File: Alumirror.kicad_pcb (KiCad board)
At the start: 2 copper layers, 139.7 x 88.9 mm, 96 parts, among them J1 USB_C_Receptacle_USB2.0_16P_2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, J2 USB_C_Receptacle_USB2.0_16P_2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, J3 USB_C_Receptacle_USB2.0_16P_2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, J4 USB_C_Receptacle_USB2.0_16P_2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, K11 PG1350, K12 PG1350, K13 PG1350, K14 PG1350, K15 PG1350, K16 PG1350, K21 PG1350, K22 PG1350, K23 PG1350, K24 PG1350, K25 PG1350, K26 PG1350, K31 PG1350, K32 PG1350, K33 PG1350, K34 PG1350, K35 PG1350, K36 PG1350_1½U, K41 PG1350_1½U, K42 PG1350/SKQUCAA010, SW10 BOOT, U1 CH552T, U2 CH552T, U3 USBLC6-2P6, U4 USBLC6-2P6, U5 USBLC6-2P6, U6 USBLC6-2P6

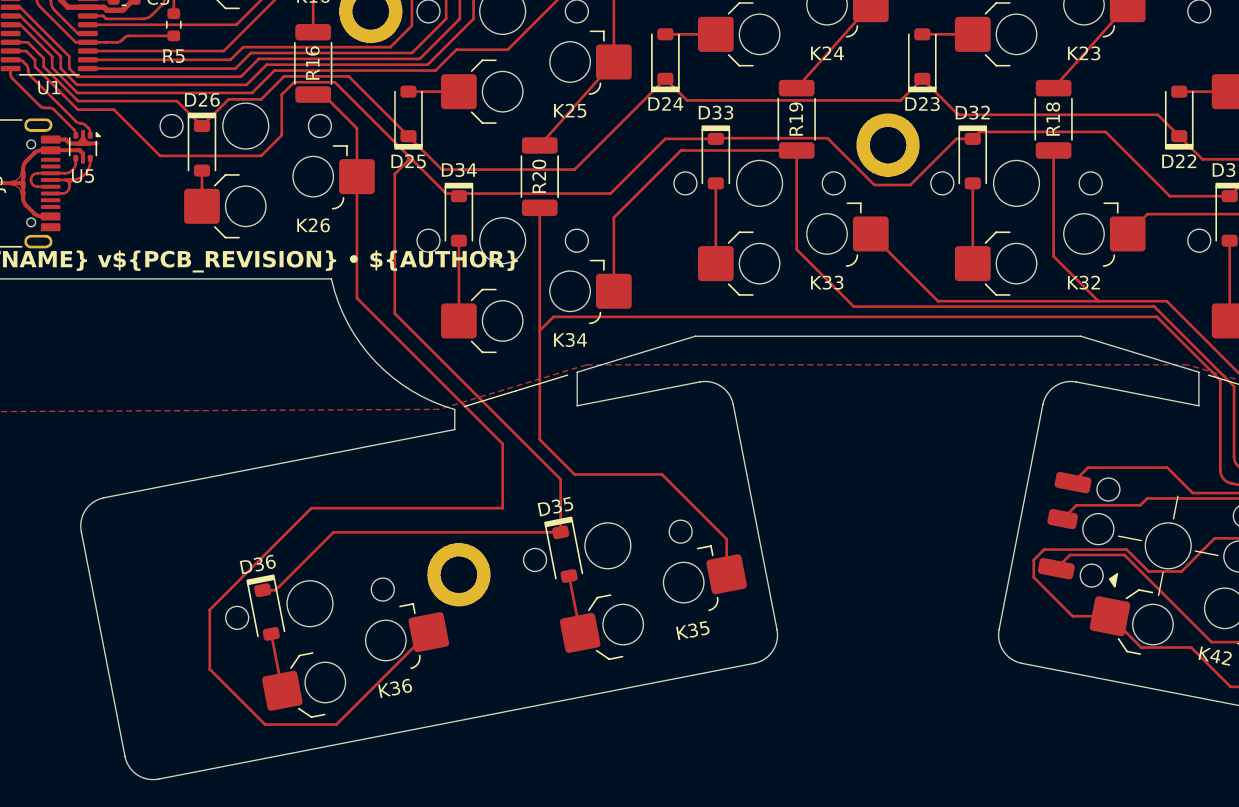
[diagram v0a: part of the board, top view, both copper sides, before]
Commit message: Clean up left thumb traces
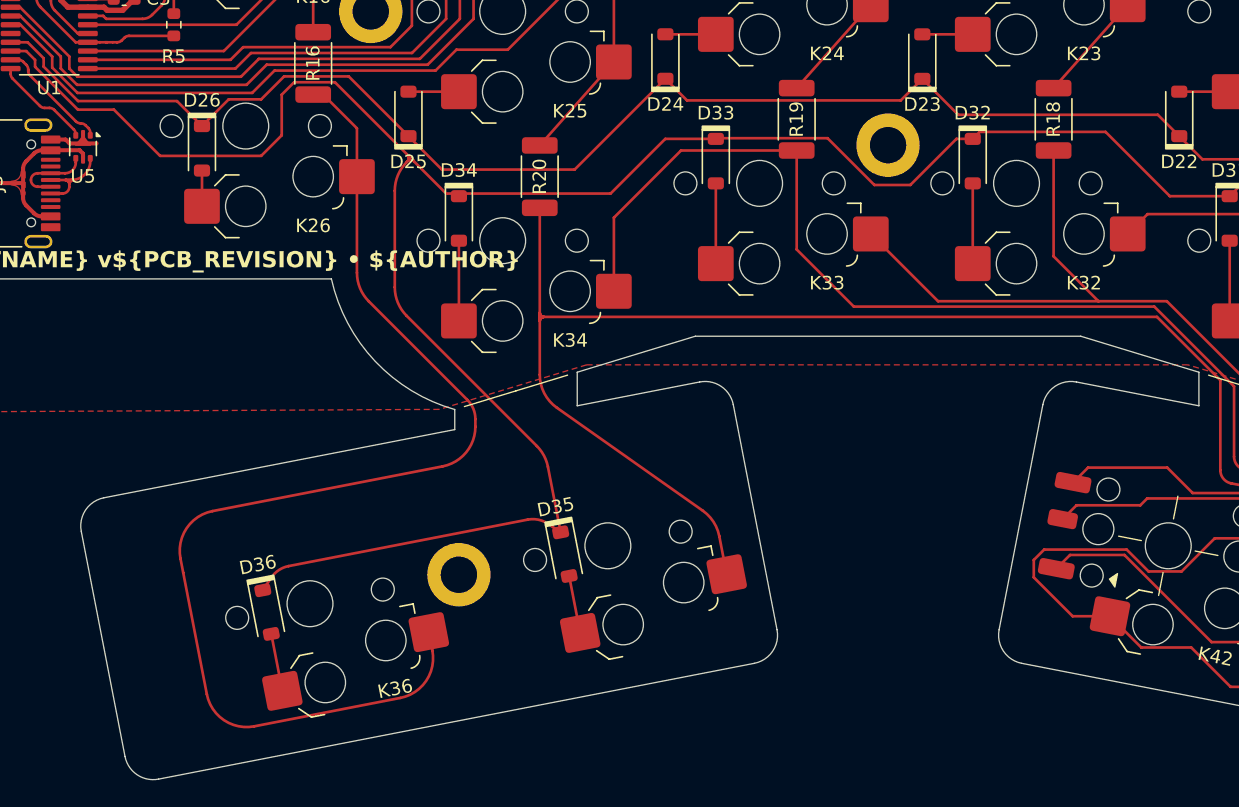
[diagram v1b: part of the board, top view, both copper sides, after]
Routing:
- net Col5T: track 113.3 -> 109.8 mm
- net Col6T: track 86.3 -> 87.1 mm
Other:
- board text added: "LED"

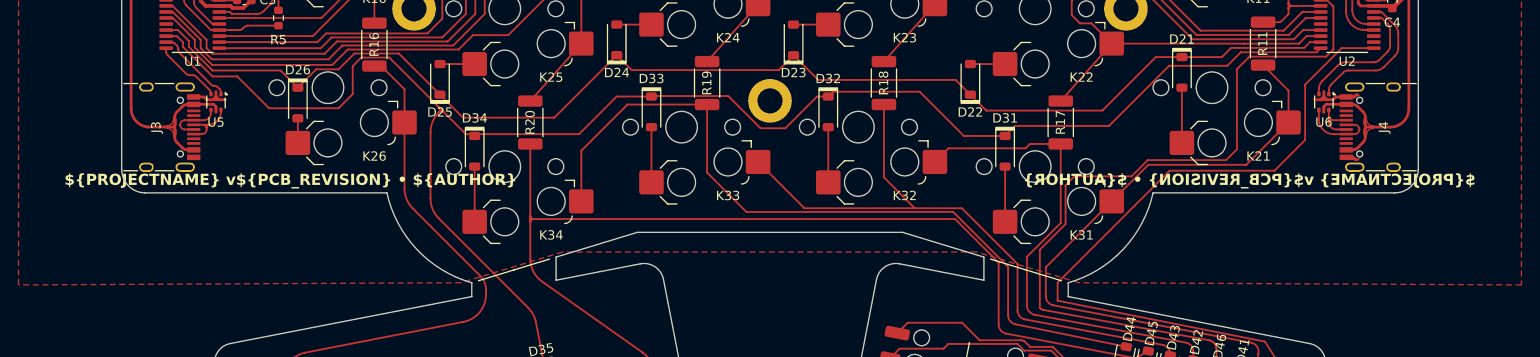
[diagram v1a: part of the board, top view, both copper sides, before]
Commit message: Switch label to mask instead of silkscreen
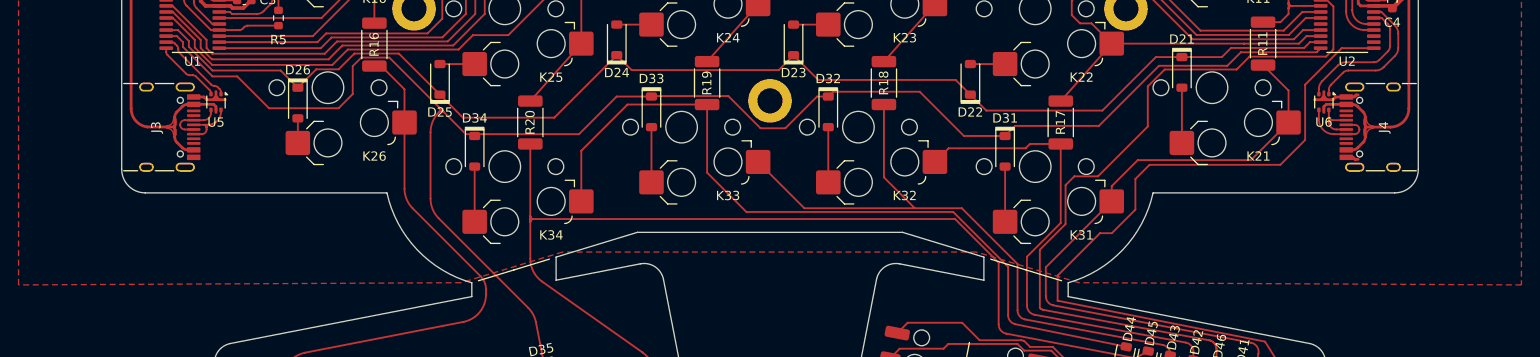
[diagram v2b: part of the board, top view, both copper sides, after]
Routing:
- net Col6: track 228.2 -> 225.7 mm
- net Row4R: track 170.3 -> 172.6 mm
- net Col1T: track 79.9 -> 80.8 mm

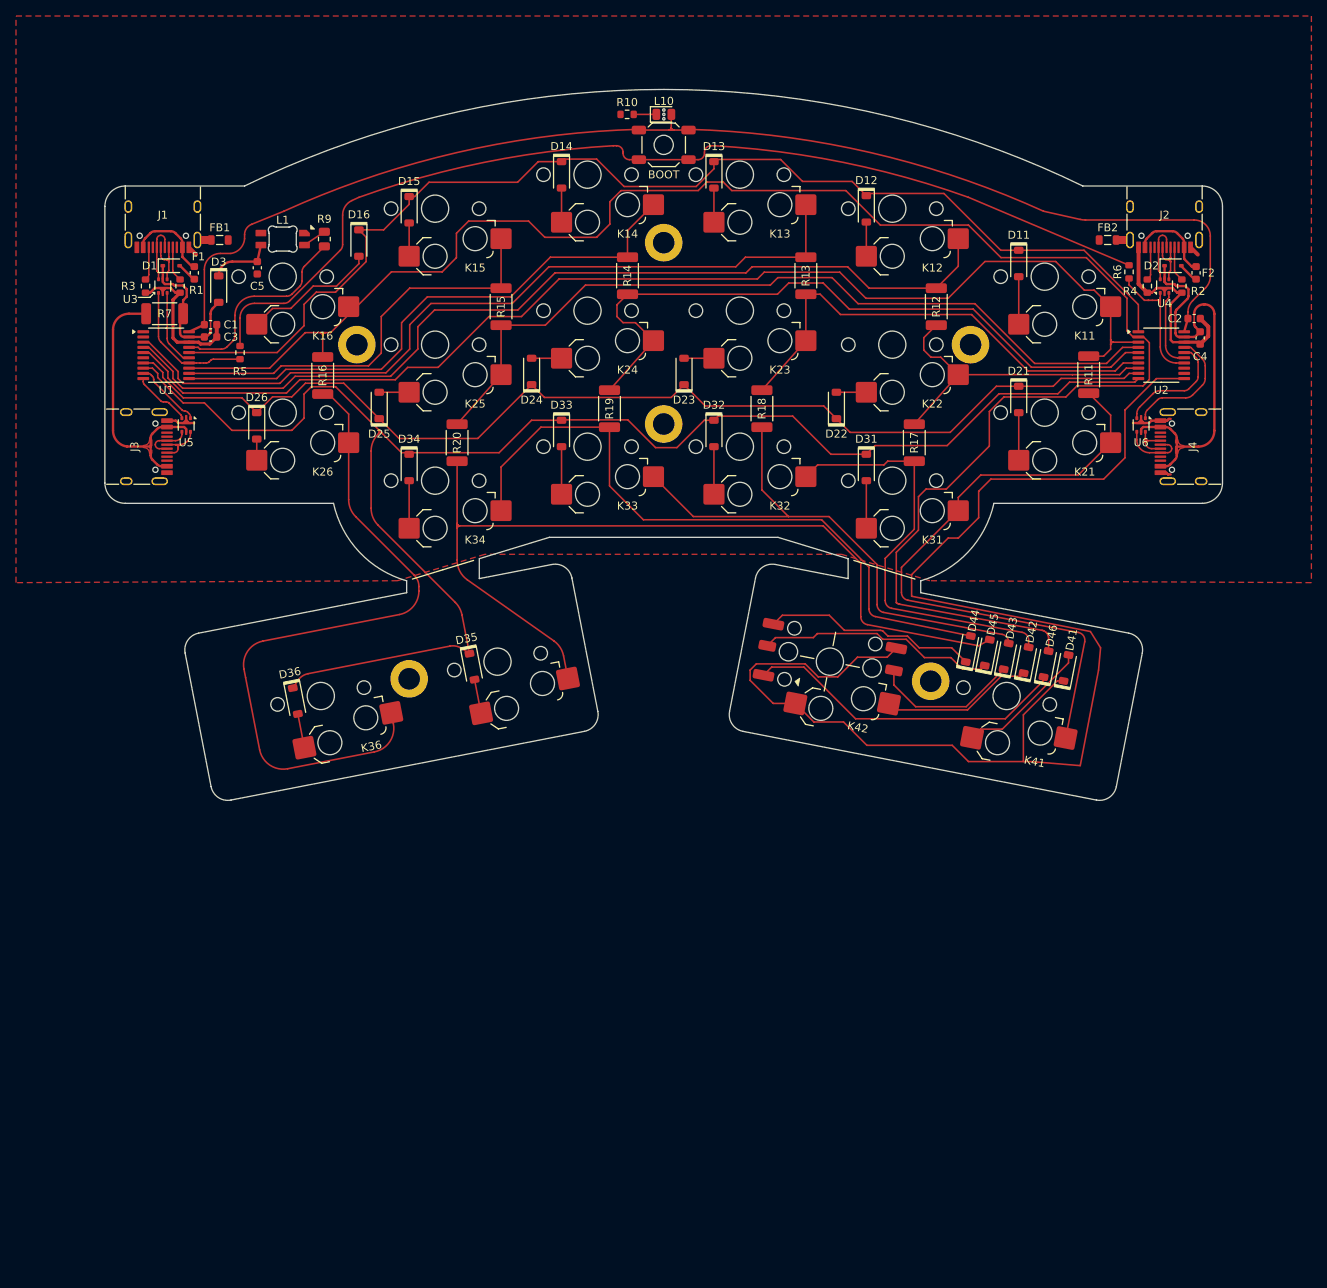
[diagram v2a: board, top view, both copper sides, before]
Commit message: Switch K22 to new “clipped” footprint
Clipped footprint has a cut-out in one of the hot-swap socket pads to avoid proximity warning with solder nut pad.
Also tweaked and rounded multiple traces.
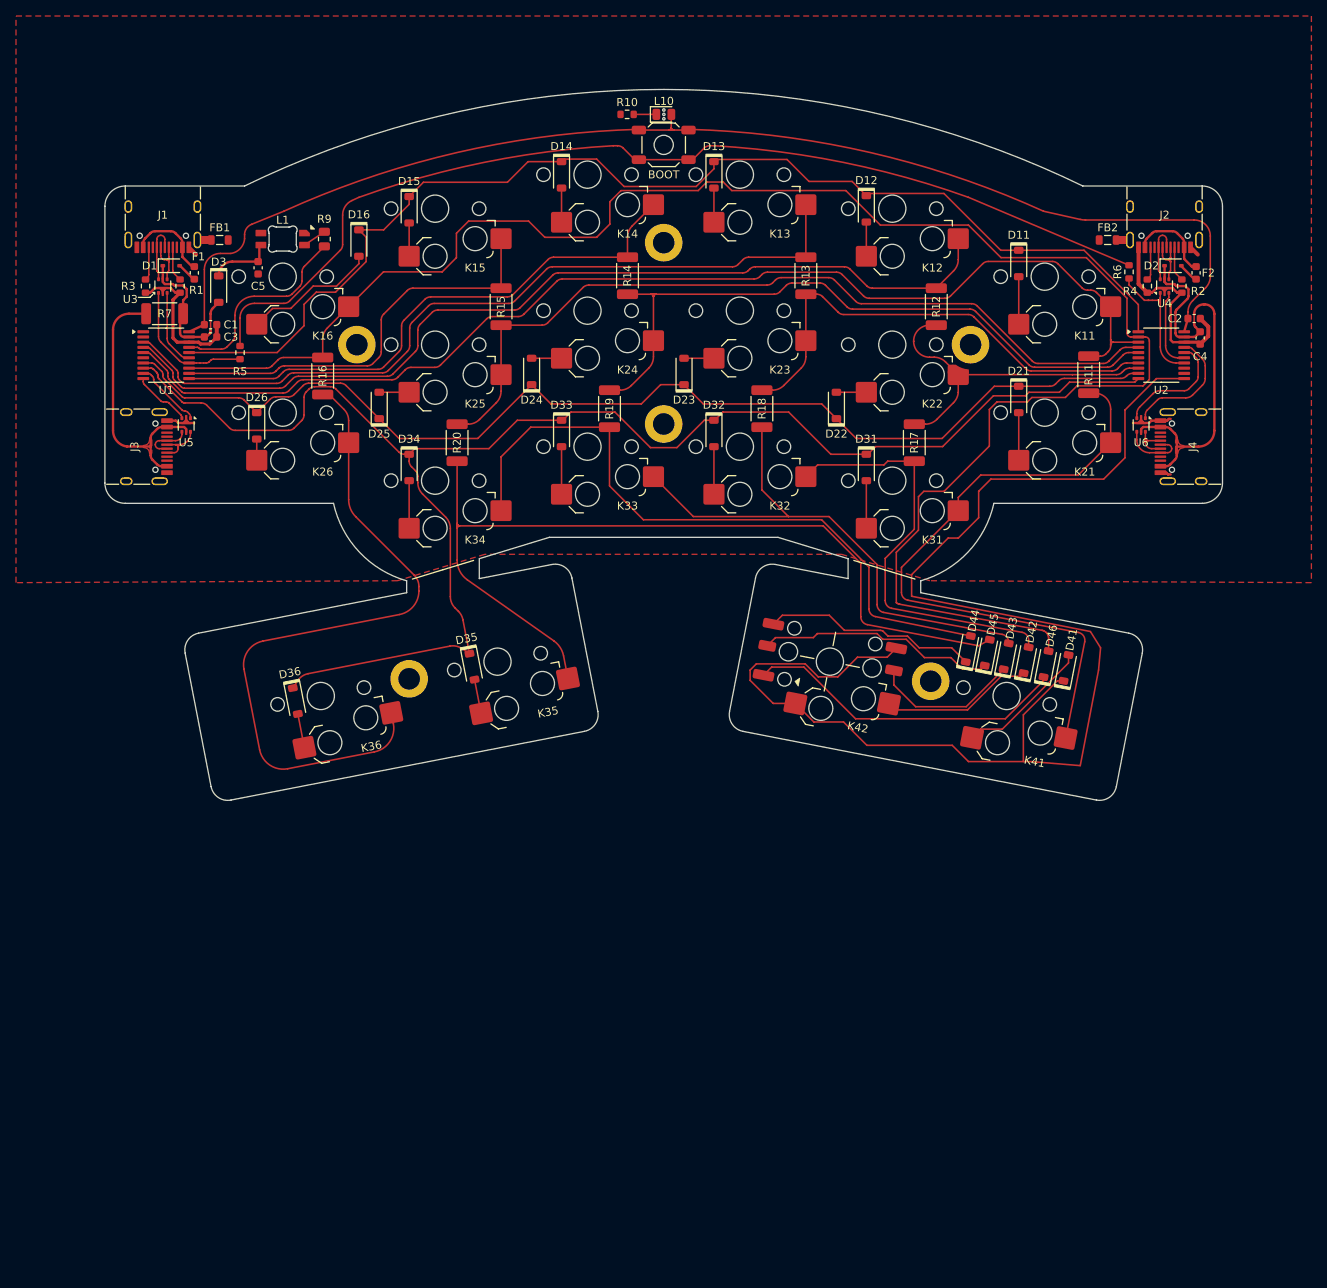
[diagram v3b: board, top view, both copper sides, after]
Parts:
- K22: footprint Project Library:SW_choc_v1_HS_CPG135001S30_1layer_1u -> Project Library:SW_choc_v1_HS_CPG135001S30_1layer_1u_clipped
- moved C5 0.11 mm to (101.7, 51.3)
- moved R16 0.06 mm to (109.8, 64.8)
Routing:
- net Row3: track 202.0 -> 197.7 mm
- net Col4R: track 87.0 -> 84.5 mm
- net Col2R: track 40.5 -> 42.5 mm
- net BOOT: track 63.8 -> 62.1 mm
- net Col1: track 146.3 -> 145.3 mm
- net Col3R: track 60.0 -> 61.0 mm
- net Col5R: track 101.9 -> 102.7 mm
- net Row2: track 141.4 -> 142.1 mm
- net Col2L: track 118.1 -> 117.4 mm
- net Col4RT: track 83.8 -> 84.5 mm
- net RX_R: track 15.5 -> 14.9 mm
- net Col3L: track 100.4 -> 99.8 mm
- net USB_L+: track 11.7 -> 11.2 mm

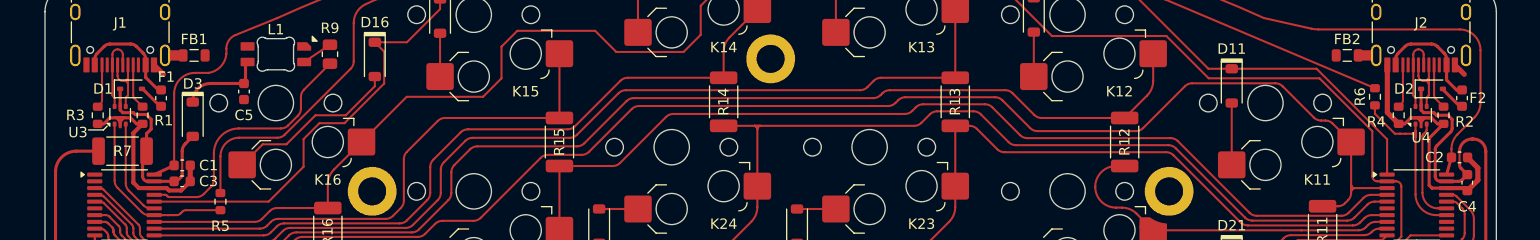
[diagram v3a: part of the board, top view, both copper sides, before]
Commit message: Add back explicit GND trace and tweak some silkscreen items
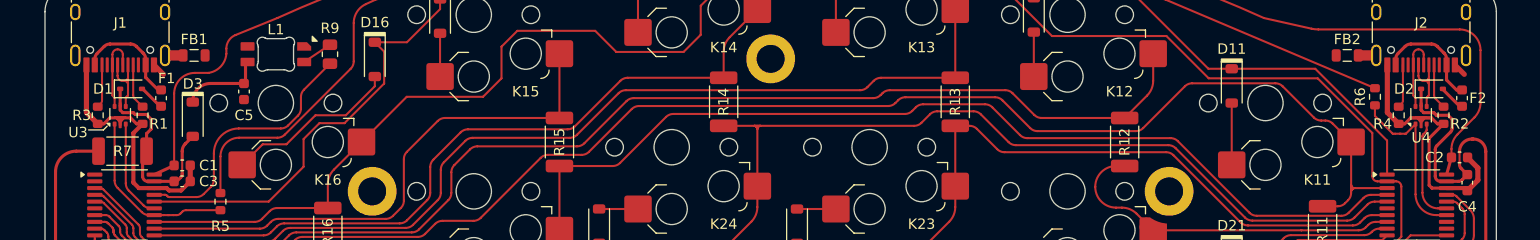
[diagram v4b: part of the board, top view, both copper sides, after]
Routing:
- net GND: track 49.7 -> 55.8 mm
- net USB_R+: track 11.5 -> 12.2 mm
